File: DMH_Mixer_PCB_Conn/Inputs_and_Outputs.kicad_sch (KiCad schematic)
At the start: 9 parts, among them J1 TS_Jack_6.35mm_Sw, J2 TS_Jack_6.35mm_Sw, J200 IDC_02x05, J3 TS_Jack_6.35mm_Sw, J4 TS_Jack_6.35mm_Sw, J5 TS_Jack_6.35mm_Sw, J50 Conn_01x08, J6 TS_Jack_6.35mm_Sw, J60 Conn_01x08

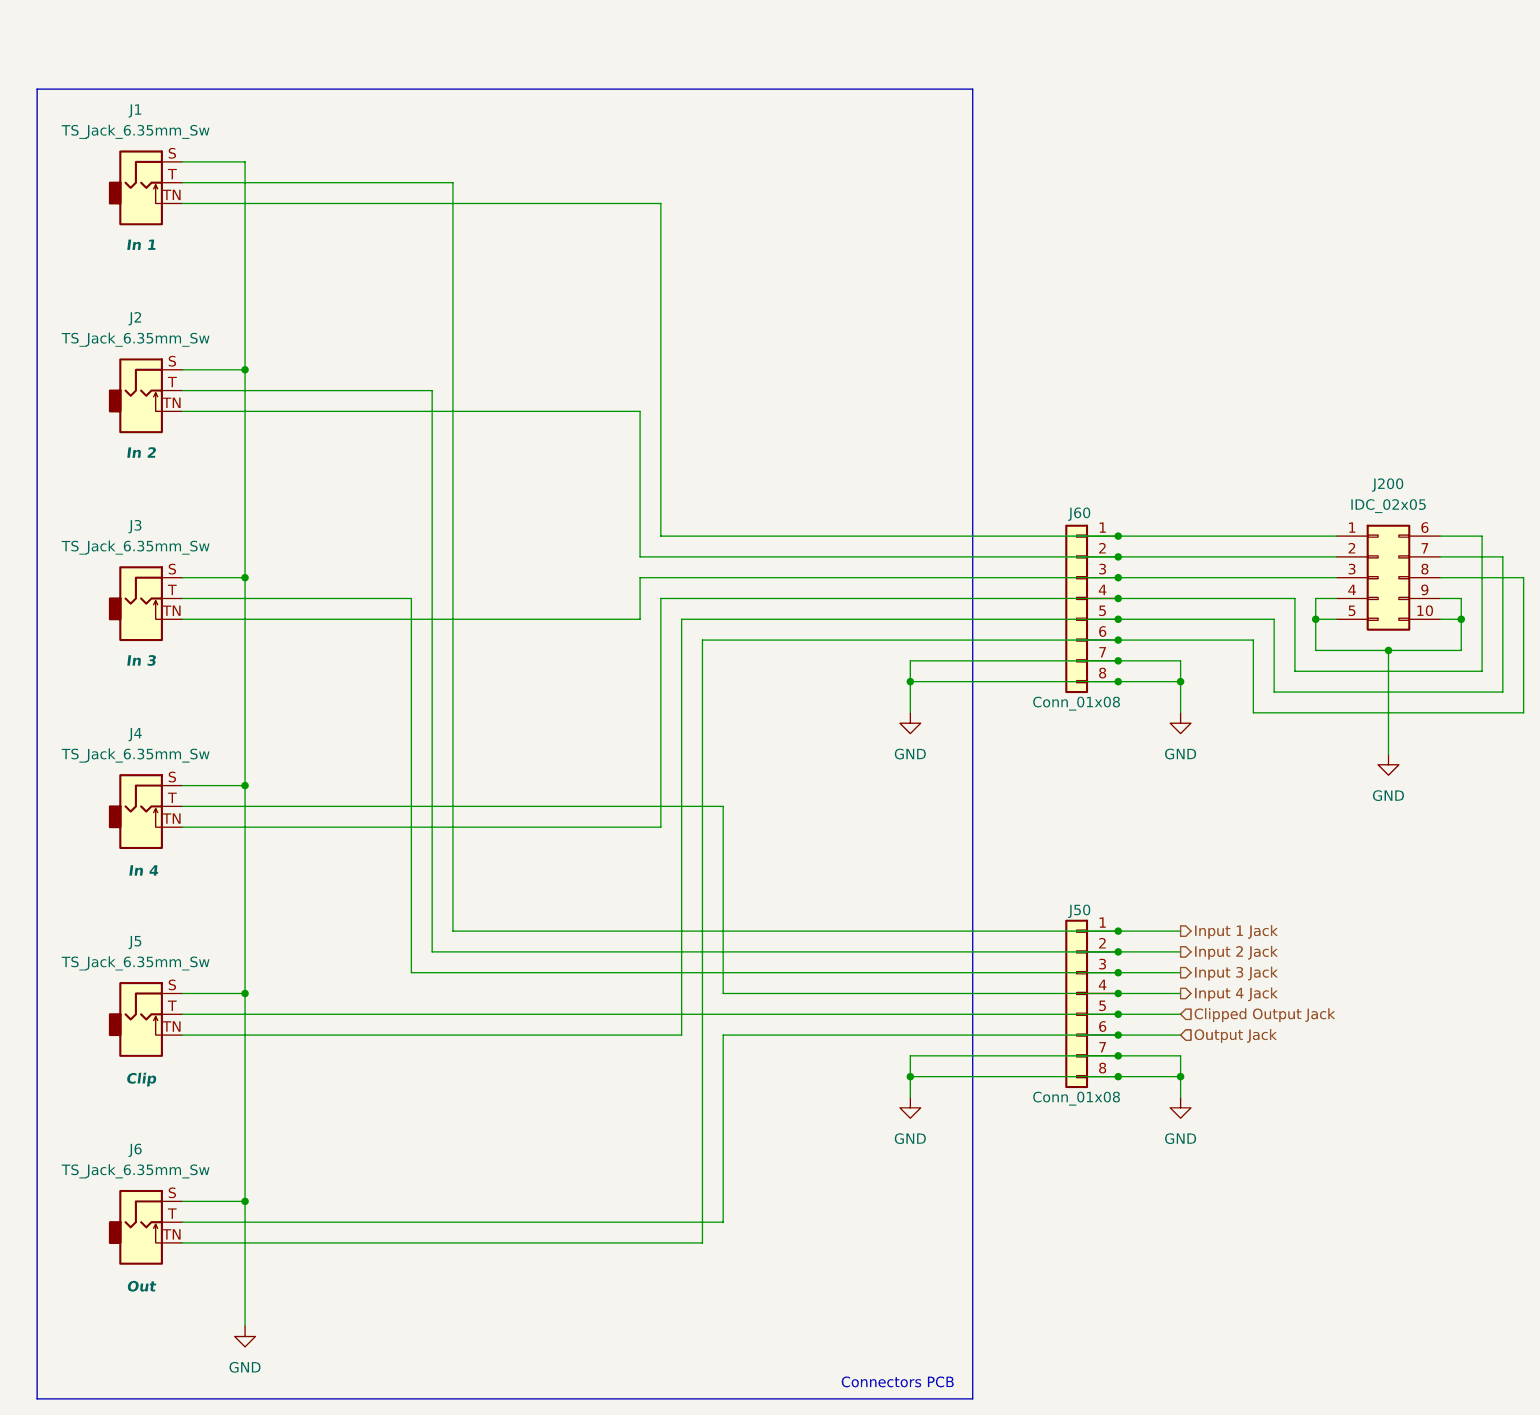
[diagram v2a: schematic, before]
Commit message: Panel and Connectors PCB ready
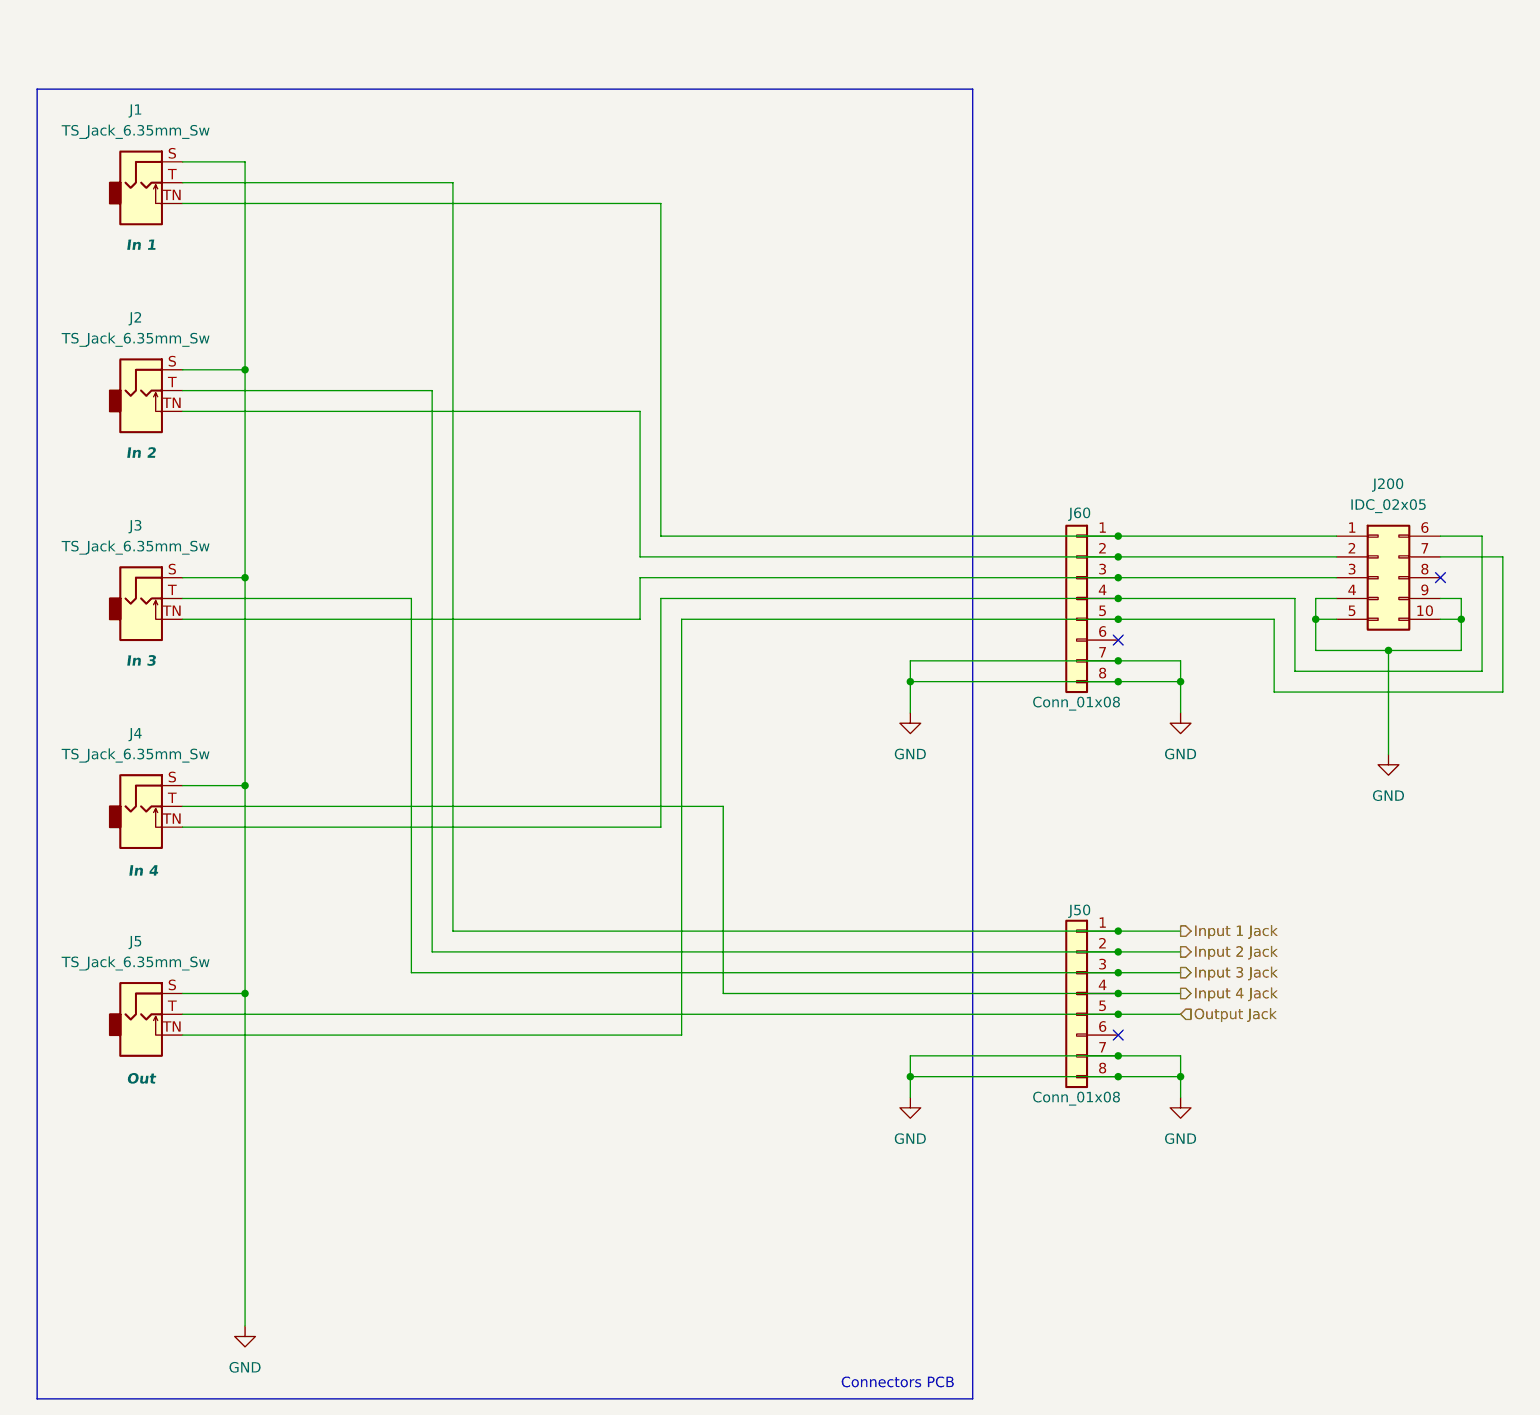
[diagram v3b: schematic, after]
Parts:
- removed J6: TS_Jack_6.35mm_Sw, SynthStuff:CUI_MJ-63052A, symbol SynthStuff:TS_Jack_6.35mm_Sw
- J5: Function Clip -> Out
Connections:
- net Clipped Output Jack is gone; now on net Output Jack: J5.T, J50.5 (Pin_5)
- net Output Jack: no longer J50.6 (Pin_6)
- net at J60.6 (Pin_6): no longer J200.8 (Pin_8)
- no-connect marks 0 -> 3
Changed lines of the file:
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@@
-	)
-	(junction
-		(at 52.07 158.75)
-		(diameter 0)
-		(color 0 0 0 0)
 	)
 	(junction
@@
 	)
 	(junction
+		(at 52.07 133.35)
+		(diameter 0)
+		(color 0 0 0 0)
+	)
+	(junction
+		(at 158.75 133.35)
+		(diameter 0)
+		(color 0 0 0 0)
+	)
+	(junction
+		(at 158.75 87.63)
+		(diameter 0)
+		(color 0 0 0 0)
+	)
+	(junction
+		(at 158.75 143.51)
+		(diameter 0)
+		(color 0 0 0 0)
+	)
+	(junction
+		(at 200.66 87.63)
+		(diameter 0)
+		(color 0 0 0 0)
+	)
+	(junction
+		(at 182.88 87.63)
+		(diameter 0)
+		(color 0 0 0 0)
+	)
+	(junction
+		(at 158.75 135.89)
+		(diameter 0)
+		(color 0 0 0 0)
+	)
+	(junction
+		(at 133.35 95.25)
+		(diameter 0)
+		(color 0 0 0 0)
+	)
+	(junction
+		(at 158.75 130.81)
+		(diameter 0)
+		(color 0 0 0 0)
+	)
+	(junction
+		(at 52.07 57.15)
+		(diameter 0)
+		(color 0 0 0 0)
+	)
+	(junction
+		(at 158.75 128.27)
+		(diameter 0)
+		(color 0 0 0 0)
+	)
+	(junction
+		(at 158.75 80.01)
+		(diameter 0)
+		(color 0 0 0 0)
+	)
+	(junction
+		(at 166.37 143.51)
+		(diameter 0)
+		(color 0 0 0 0)
+	)
+	(no_connect
 		(at 158.75 90.17)
-		(diameter 0)
-		(color 0 0 0 0)
-	)
-	(junction
-		(at 52.07 133.35)
-		(diameter 0)
-		(color 0 0 0 0)
-	)
-	(junction
-		(at 158.75 133.35)
-		(diameter 0)
-		(color 0 0 0 0)
-	)
-	(junction
-		(at 158.75 87.63)
-		(diameter 0)
-		(color 0 0 0 0)
-	)
-	(junction
-		(at 158.75 143.51)
-		(diameter 0)
-		(color 0 0 0 0)
-	)
-	(junction
-		(at 200.66 87.63)
-		(diameter 0)
-		(color 0 0 0 0)
-	)
-	(junction
-		(at 182.88 87.63)
-		(diameter 0)
-		(color 0 0 0 0)
-	)
-	(junction
-		(at 158.75 135.89)
-		(diameter 0)
-		(color 0 0 0 0)
-	)
-	(junction
-		(at 133.35 95.25)
-		(diameter 0)
-		(color 0 0 0 0)
-	)
-	(junction
-		(at 158.75 130.81)
-		(diameter 0)
-		(color 0 0 0 0)
-	)
-	(junction
-		(at 52.07 57.15)
-		(diameter 0)
-		(color 0 0 0 0)
-	)
-	(junction
-		(at 158.75 128.27)
-		(diameter 0)
-		(color 0 0 0 0)
-	)
-	(junction
-		(at 158.75 80.01)
-		(diameter 0)
-		(color 0 0 0 0)
-	)
-	(junction
-		(at 166.37 143.51)
-		(diameter 0)
-		(color 0 0 0 0)
-	)
-	(junction
+	)
+	(no_connect
+		(at 198.12 82.55)
+	)
+	(no_connect
 		(at 158.75 138.43)
-		(diameter 0)
-		(color 0 0 0 0)
 	)
 	(wire
@@
 	(wire
 		(pts
-			(xy 44.45 163.83) (xy 107.95 163.83)
-		)
-		(stroke
-			(width 0)
-			(type default)
-		)
-	)
-	(wire
-		(pts
 			(xy 77.47 34.29) (xy 77.47 125.73)
 		)
@@
 	(wire
 		(pts
-			(xy 208.28 82.55) (xy 198.12 82.55)
-		)
-		(stroke
-			(width 0)
-			(type default)
-		)
-	)
-	(wire
-		(pts
 			(xy 177.8 87.63) (xy 177.8 96.52)
 		)
@@
 	(wire
 		(pts
-			(xy 52.07 158.75) (xy 52.07 173.99)
-		)
-		(stroke
-			(width 0)
-			(type default)
-		)
-	)
-	(wire
-		(pts
 			(xy 44.45 138.43) (xy 105.41 138.43)
 		)
@@
 	(wire
 		(pts
-			(xy 175.26 99.06) (xy 208.28 99.06)
-		)
-		(stroke
-			(width 0)
-			(type default)
-		)
-	)
-	(wire
-		(pts
-			(xy 110.49 138.43) (xy 158.75 138.43)
-		)
-		(stroke
-			(width 0)
-			(type default)
-		)
-	)
-	(wire
-		(pts
 			(xy 198.12 87.63) (xy 200.66 87.63)
 		)
@@
 	(wire
 		(pts
-			(xy 158.75 90.17) (xy 175.26 90.17)
-		)
-		(stroke
-			(width 0)
-			(type default)
-		)
-	)
-	(wire
-		(pts
 			(xy 133.35 95.25) (xy 133.35 92.71)
 		)
@@
 	(wire
 		(pts
-			(xy 110.49 161.29) (xy 110.49 138.43)
-		)
-		(stroke
-			(width 0)
-			(type default)
-		)
-	)
-	(wire
-		(pts
 			(xy 133.35 143.51) (xy 133.35 140.97)
 		)
@@
 	(wire
 		(pts
-			(xy 208.28 99.06) (xy 208.28 82.55)
-		)
-		(stroke
-			(width 0)
-			(type default)
-		)
-	)
-	(wire
-		(pts
 			(xy 44.45 59.69) (xy 74.93 59.69)
 		)
@@
 	(wire
 		(pts
-			(xy 44.45 158.75) (xy 52.07 158.75)
-		)
-		(stroke
-			(width 0)
-			(type default)
-		)
-	)
-	(wire
-		(pts
 			(xy 44.45 62.23) (xy 100.33 62.23)
 		)
@@
 	(wire
 		(pts
-			(xy 107.95 90.17) (xy 158.75 90.17)
-		)
-		(stroke
-			(width 0)
-			(type default)
-		)
-	)
-	(wire
-		(pts
 			(xy 133.35 92.71) (xy 158.75 92.71)
 		)
@@
 	(wire
 		(pts
-			(xy 44.45 161.29) (xy 110.49 161.29)
-		)
-		(stroke
-			(width 0)
-			(type default)
-		)
-	)
-	(wire
-		(pts
 			(xy 44.45 82.55) (xy 52.07 82.55)
 		)
@@
 	(wire
 		(pts
-			(xy 107.95 163.83) (xy 107.95 90.17)
-		)
-		(stroke
-			(width 0)
-			(type default)
-		)
-	)
-	(wire
-		(pts
 			(xy 105.41 138.43) (xy 105.41 87.63)
 		)
@@
 	(wire
 		(pts
-			(xy 158.75 138.43) (xy 166.37 138.43)
-		)
-		(stroke
-			(width 0)
-			(type default)
-		)
-	)
-	(wire
-		(pts
 			(xy 100.33 80.01) (xy 158.75 80.01)
 		)
@@
 	(wire
 		(pts
-			(xy 175.26 90.17) (xy 175.26 99.06)
-		)
-		(stroke
-			(width 0)
-			(type default)
-		)
-	)
-	(wire
-		(pts
 			(xy 52.07 31.75) (xy 44.45 31.75)
 		)
@@
 	(wire
 		(pts
-			(xy 52.07 133.35) (xy 52.07 158.75)
+			(xy 52.07 133.35) (xy 52.07 173.99)
 		)
 		(stroke
@@
 		)
 	)
-	(hierarchical_label "Clipped Output Jack"
+	(hierarchical_label "Output Jack"
 		(shape input)
 		(at 166.37 135.89 0)
-		(fields_autoplaced yes)
-		(effects
-			(font
-				(size 1.27 1.27)
-			)
-			(justify left)
-		)
-	)
-	(hierarchical_label "Output Jack"
-		(shape input)
-		(at 166.37 138.43 0)
 		(fields_autoplaced yes)
 		(effects
@@
 				(path "/58f4306d-5387-4983-bb08-41a2313fd315/ce3fef8b-9f1d-4178-b50b-4a046c030679"
 					(reference "J1")
-					(unit 1)
-				)
-			)
-		)
-	)
-	(symbol
-		(lib_id "SynthStuff:TS_Jack_6.35mm_Sw")
-		(at 39.37 161.29 0)
-		(unit 1)
-		(exclude_from_sim no)
-		(in_bom yes)
-		(on_board yes)
-		(dnp no)
-		(property "Reference" "J6"
-			(at 38.735 152.4 0)
-			(effects
-				(font
-					(size 1.27 1.27)
-				)
-			)
-		)
-		(property "Value" "TS_Jack_6.35mm_Sw"
-			(at 38.735 154.94 0)
-			(effects
-				(font
-					(size 1.27 1.27)
-				)
-			)
-		)
-		(property "Footprint" "SynthStuff:CUI_MJ-63052A"
-			(at 39.37 161.29 0)
-			(effects
-				(font
-					(size 1.27 1.27)
-				)
-				(hide yes)
-			)
-		)
-		(property "Datasheet" "~"
-			(at 39.37 161.29 0)
-			(effects
-				(font
-					(size 1.27 1.27)
-				)
-				(hide yes)
-			)
-		)
-		(property "Description" "Audio Jack, 2 Poles (Mono / TS), Switched T Pole (Normalling), 6.35mm, 1/4inch"
-			(at 39.37 161.29 0)
-			(effects
-				(font
-					(size 1.27 1.27)
-				)
-				(hide yes)
-			)
-		)
-		(property "Function" "Out"
-			(at 39.37 169.164 0)
-			(effects
-				(font
-					(size 1.27 1.27)
-					(thickness 0.254)
-					(bold yes)
-					(italic yes)
-				)
-			)
-		)
-		(pin "T"
-		)
-		(pin "TN"
-		)
-		(pin "S"
-		)
-		(instances
-			(project "DMH_Mixer_PCB_Conn"
-				(path "/58f4306d-5387-4983-bb08-41a2313fd315/ce3fef8b-9f1d-4178-b50b-4a046c030679"
-					(reference "J6")
 					(unit 1)
 				)
@@
 			)
 		)
-		(property "Function" "Clip"
+		(property "Function" "Out"
 			(at 39.37 143.764 0)
 			(effects
